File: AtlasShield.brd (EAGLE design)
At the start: 7 parts, among them J1 AVR_SPI_PRG_6NS

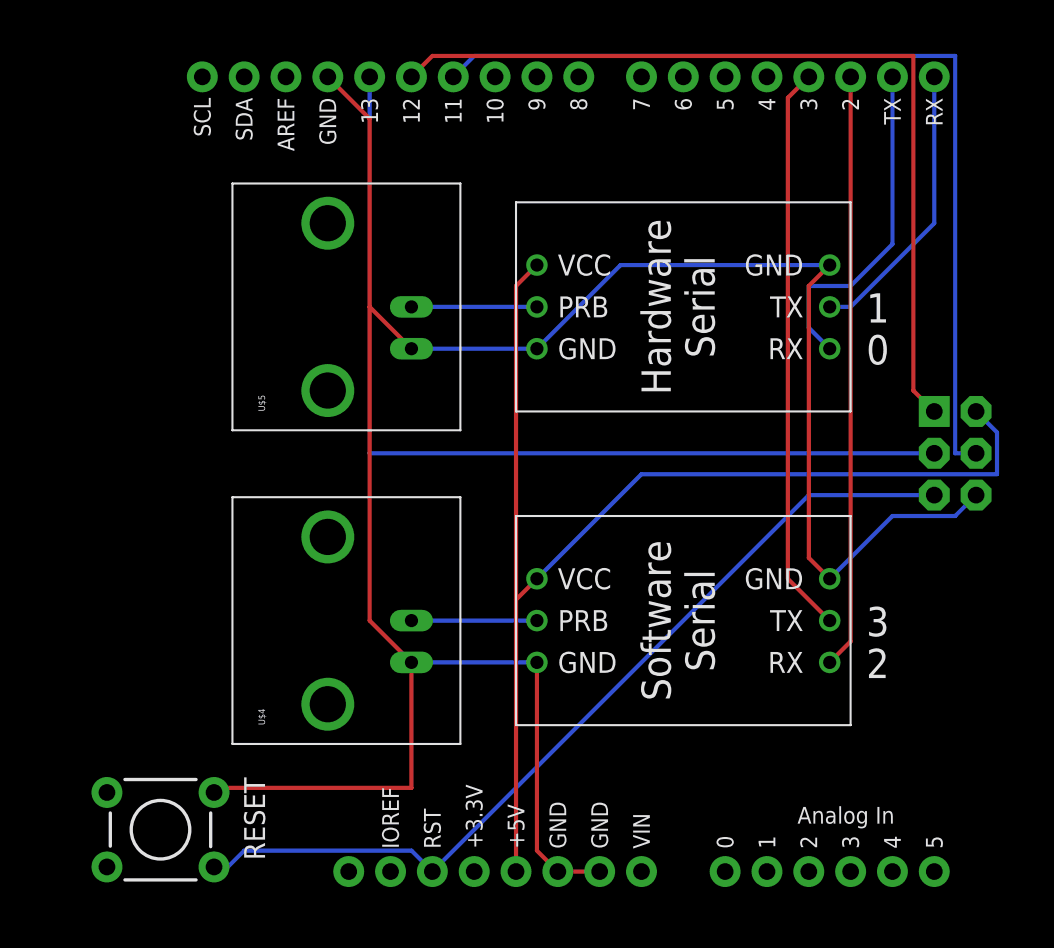
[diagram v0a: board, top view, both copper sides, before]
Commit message: added DPDT switches to optionally send either sensor to the SPI bus
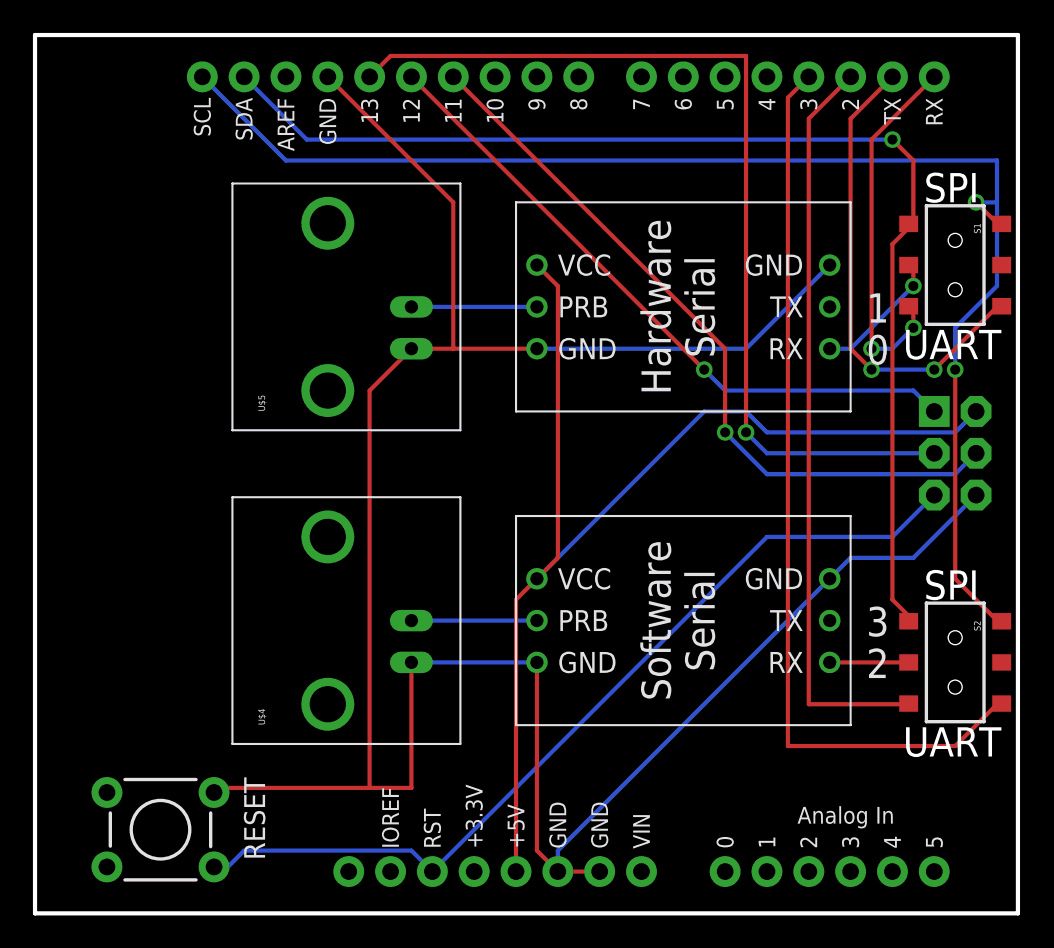
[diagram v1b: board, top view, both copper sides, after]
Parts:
- added S1, S2: DPDT, SparkFun-Electromechanical:AYZ0202
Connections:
- removed net N$1: U$1.RX, U$2.TX
- removed net N$2: U$1.TX, U$2.RX
- removed net N$3: U$1.D2, U$3.RX
- removed net N$4: U$1.D3, U$3.TX
- new net RX_0: S1.6, U$1.RX
- new net RX_2: S2.6, U$1.D2
- new net RX_HARD: S1.5, U$2.RX
- new net RX_SOFT: S2.5, U$3.RX
- new net SCL: S1.1, S2.1, U$1.SCL
- new net SDA: S1.4, S2.4, U$1.SDA
- new net TX_1: S1.3, U$1.TX
- new net TX_3: S2.3, U$1.D3
- new net TX_HARD: S1.2, U$2.TX
- new net TX_SOFT: S2.2, U$3.TX
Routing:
- net SCL: track 0.00 -> 84.1 mm, vias 0 -> 2
- net SDA: track 0.00 -> 72.3 mm, vias 0 -> 1
- net TX_3: track 0.00 -> 55.2 mm
- net RX_2: track 0.00 -> 45.8 mm
- net N$3: track 36.1 -> 0.00 mm
- net N$4: track 34.6 -> 0.00 mm
- net TX_1: track 0.00 -> 28.8 mm, vias 0 -> 2
- net RX_0: track 0.00 -> 22.7 mm, vias 0 -> 2
- net N$2: track 20.6 -> 0.00 mm
- net N$1: track 17.3 -> 0.00 mm
- net N$7: track 53.1 -> 40.2 mm, vias 0 -> 1
- net N$6: track 56.4 -> 45.2 mm, vias 0 -> 1
- net GND: track 142.9 -> 153.6 mm
- net RX_HARD: track 0.00 -> 8.21 mm, vias 0 -> 1
- net RX_SOFT: track 0.00 -> 5.08 mm
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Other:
- board outline added: 59.7 x 53.3 mm
- board text added: "SPI"
- board text added: "UART"
